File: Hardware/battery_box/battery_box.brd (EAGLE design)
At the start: 60 x 70 mm, 24 parts, among them IC1 LM2574N-5.0, U1 PIC16F506P

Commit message: Added Connectors to Schematic
Adds the DC Jacks and USB connectors and LEDs to the schematic for
mounting on PCB. Added comments to schematic and changed .gitignore
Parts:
- removed TB: 6WAYTB, inverter:TERMINAL_BLOCK
- removed X1: (no value), con-molex:22-23-2061
- added J1: CON_HEADER_PRG_PIC_ICSPA, equinox:HEADER_PRG_1X05
- added LD1: (no value), led:DUOLED-C-5MM
- added R6: (no value), rcl:R0805
- added X2: KUSBVX, con-kycon:KUSBVX
- U$2: value EQBX_PTCEQBX_PTC -> KYCON_KLDVX-0202; device eqbx_ptc:EQBX_PTC -> equinox:KYCON_KLVDX_2020_B
- U$3: value EQBX_FUSEEQBX_FUSE -> KYCON_KLDVX-0202; device eqbx_fuse:EQBX_FUSE -> equinox:KYCON_KLVDX_2020_B
- moved U$3 76.4 mm to (7.85, -22.1)
- moved U$2 64.5 mm to (7.85, -10.3), turned to 0 degrees
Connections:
- removed net N$10: U1.4, X1.1
- removed net N$14: R8.1, TB.P$6
- removed net N$19: TB.P$1, U$2.PTC-
- removed net N$5: U1.13, X1.4
- removed net N$6: CIN_PIC.1, D1.C, R13.1, U1.1, X1.2
- removed net N$7: U1.12, X1.5
- new net MCLR-: J1.1, U1.4
- new net PGC: J1.5, U1.12
- new net PGD: J1.4, U1.13
- new net VDD: CIN_PIC.1, D1.C, J1.2, R13.1, U1.1
- new net V_BATT: DCHARGE.NEGATIVE, PMOS.S, R1.2, R13.2, R4.1
- net GND: now also J1.3, LD1.C, R6.1, X2.4, X2.M1, X2.M2; no longer TB.P$4, X1.3
- net N$1: now also R6.2, U$2.2, U$2.3, U$3.2, U$3.3; no longer U$2.PTC+, U$3.-, U$3.-1
- net N$17: now also LD1.AR, R8.1; no longer COUT.1, IC1.1, INDUCTOR.P$2, TB.P$3
- net N$2: now also LD1.AX; no longer TB.P$5
- net N$20: now also U$2.1, U$3.1; no longer TB.P$2
- net N$4: now also COUT.1, IC1.1, INDUCTOR.P$2, X2.1; no longer DCHARGE.NEGATIVE, PMOS.S, R1.2, R13.2, R4.1, U$3.+, U$3.+1
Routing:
- net N$17: track 105.5 -> 0.00 mm
- net N$10: track 58.3 -> 0.00 mm
- net MCLR-: track 0.00 -> 57.5 mm
- net N$4: track 50.4 -> 0.00 mm
- net V_BATT: track 0.00 -> 48.5 mm
- net N$6: track 34.0 -> 0.00 mm
- net VDD: track 0.00 -> 32.7 mm
- net N$19: track 18.8 -> 0.00 mm
- net N$7: track 17.5 -> 0.00 mm
- net N$5: track 17.5 -> 0.00 mm
- net PGD: track 0.00 -> 16.3 mm
- net PGC: track 0.00 -> 16.3 mm
- net N$1: track 15.3 -> 0.00 mm
- net N$14: track 7.84 -> 0.00 mm
- net N$20: track 87.9 -> 86.8 mm

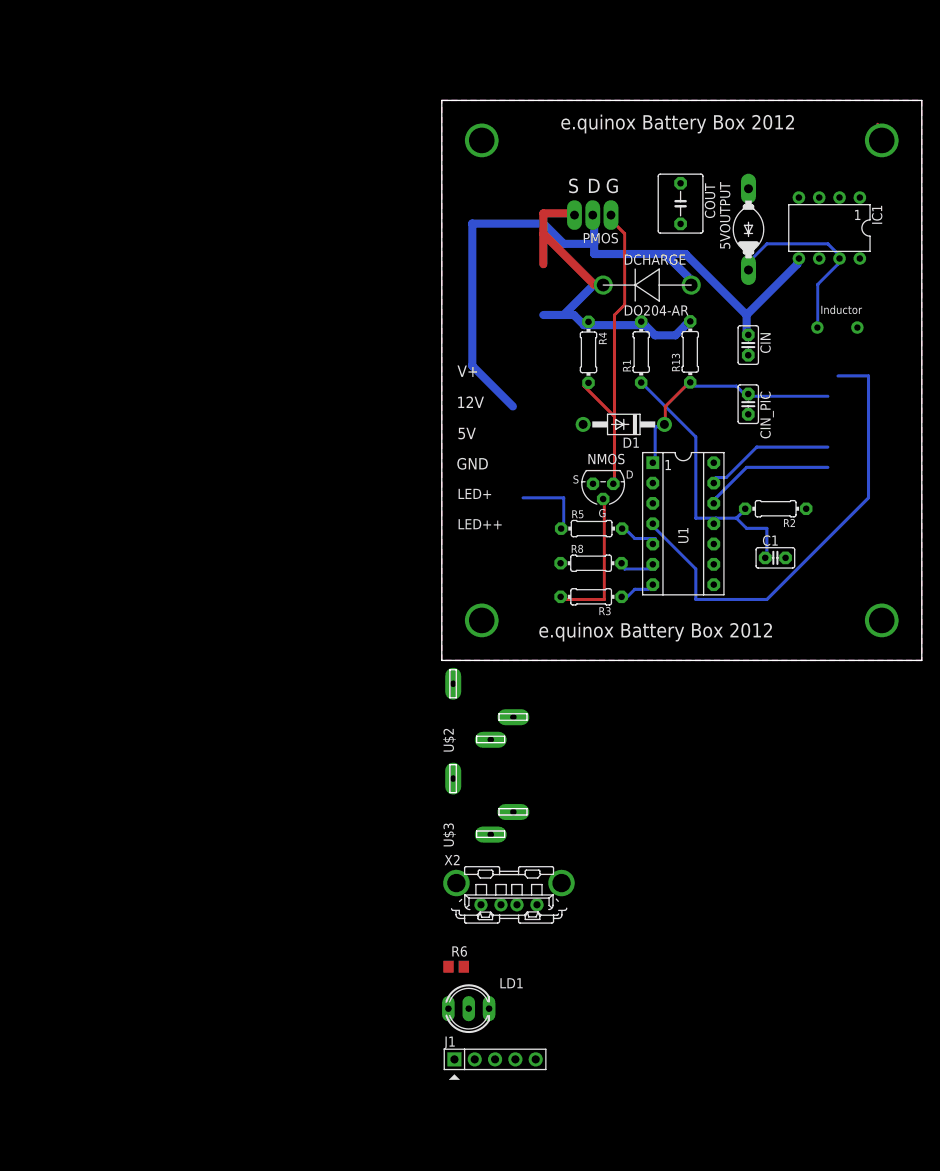
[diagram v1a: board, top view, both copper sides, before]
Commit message: Added cooments to fix problems identified
Problems identified during 2013 Jan trip have added as comments.
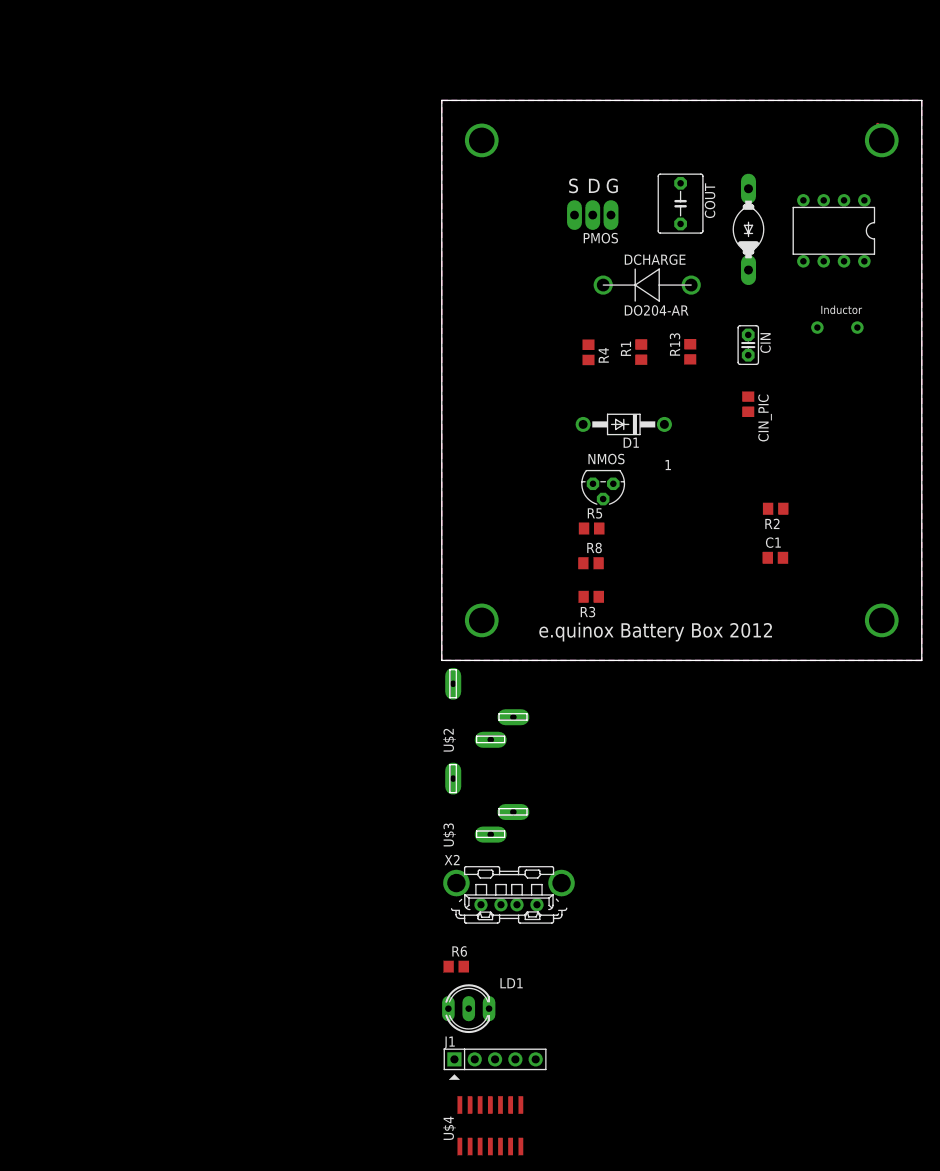
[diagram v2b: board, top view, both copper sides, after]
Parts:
- removed U1: PIC16F506P, microchip:DIP-14
- added U$4: PIC16F1503SOIC, equinox:SO-14
- C1: device capacitor-wima:C2.5-2 -> rcl:C0805
- CIN_PIC: value 22u -> 1u; device capacitor-wima:C2.5-2 -> rcl:C0805
- R1, R13, R2, R3, R4, R5, R8: device rcl:0204/7 -> rcl:R0805
- moved U$1 18.7 mm to (69.7, 12.5)
- moved IC1 0.66 mm to (49.0, 53.7)
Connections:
- removed net N$12: R3.1, U1.7
- new net N$5: R3.2, U$4.7
- net GND: now also U$4.14; no longer U1.14
- net MCLR-: no longer U1.4
- net N$13: now also R3.1; no longer R3.2
- net N$15: now also U$4.6; no longer U1.6
- net N$3: now also U$4.11; no longer U1.11
- net N$8: now also U$4.5; no longer U1.5
- net PGC: no longer U1.12
- net PGD: no longer U1.13
- net VDD: now also U$4.1; no longer U1.1
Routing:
- net N$20: track 86.8 -> 0.00 mm
- net MCLR-: track 57.5 -> 0.00 mm
- net V_BATT: track 48.5 -> 0.00 mm
- net N$9: track 40.8 -> 0.00 mm
- net N$3: track 36.0 -> 0.00 mm
- net VDD: track 32.7 -> 0.00 mm
- net N$11: track 24.1 -> 0.00 mm
- net N$13: track 18.5 -> 0.00 mm
- net PGD: track 16.3 -> 0.00 mm
- net PGC: track 16.3 -> 0.00 mm
- net N$2: track 9.21 -> 0.00 mm
- net N$12: track 5.49 -> 0.00 mm
- net N$8: track 5.41 -> 0.00 mm
- net N$15: track 5.28 -> 0.00 mm
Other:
- board text removed: "12V"
- board text removed: "5V"
- board text removed: "GND"
- board text removed: "LED+"
- board text removed: "LED++"
- board text removed: "V+"

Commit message: Added the Connector Test PCB
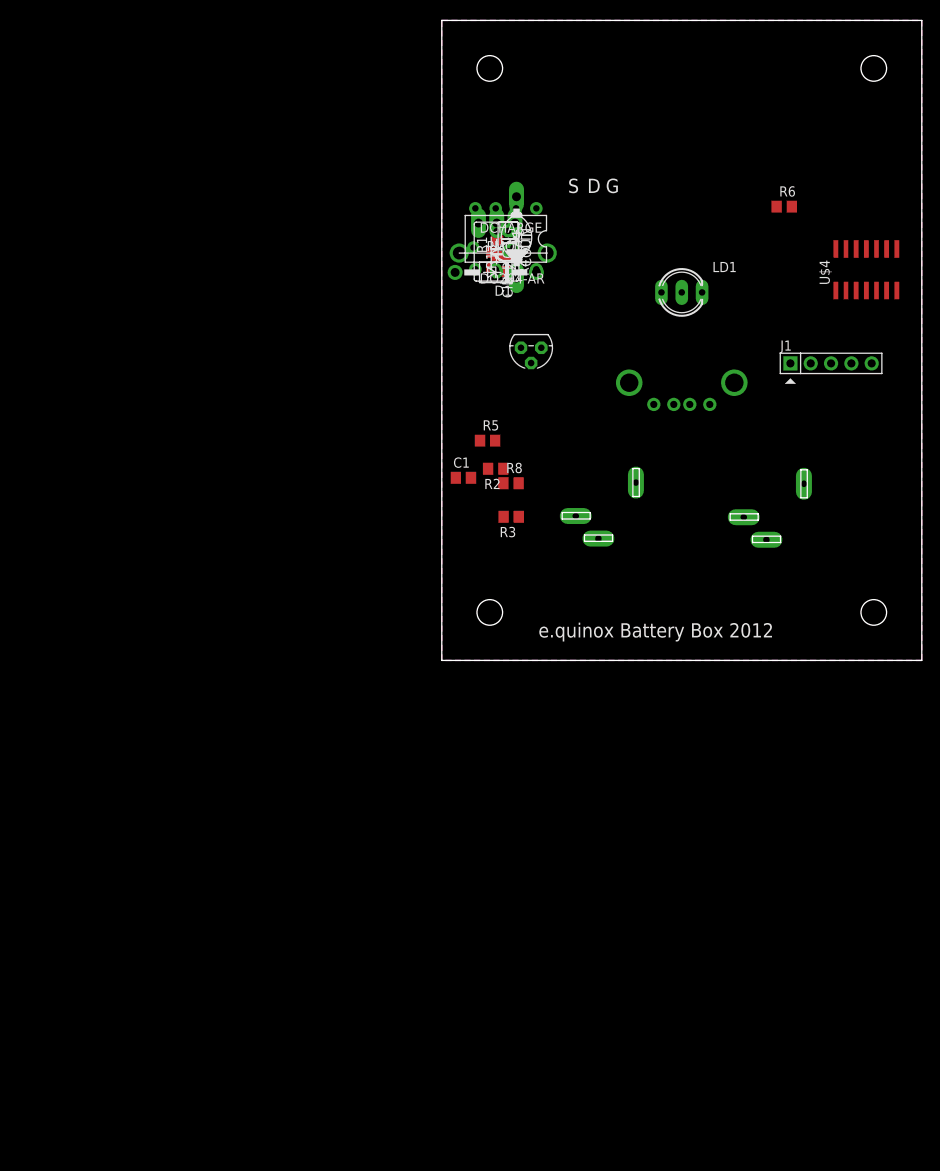
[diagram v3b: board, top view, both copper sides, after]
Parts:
- added U$5, U$6, U$7, U$8: PCB_MOUNT_RICHO, equinox:PCBMOUNT
- moved U$4 116.9 mm to (53.1, 48.8)
- moved R6 103.5 mm to (42.8, 56.7)
- moved J1 96.6 mm to (48.7, 37.1)
- moved LD1 93.4 mm to (30.0, 46.0)
- moved U$1 86.4 mm to (5.73, 70.5)
- moved X2 66.2 mm to (30.0, 32.0), flipped to the bottom
- moved INDUCTOR 44.1 mm to (6.45, 51.6)
- moved IC1 41.0 mm to (8.01, 52.7)
- moved C1 40.3 mm to (2.70, 22.8)
- moved U$2 39.8 mm to (38.9, 14.7), flipped to the bottom
- moved U$3 38.3 mm to (17.9, 14.9), flipped to the bottom
- moved CIN_PIC 36.7 mm to (6.31, 50.0)
- moved R2 35.4 mm to (6.74, 24.0)
- moved CIN 32.7 mm to (8.31, 52.4)
- moved 5VOUTPUT 29.0 mm to (9.34, 52.9)
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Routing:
- net N$18: track 1.50 -> 0.00 mm
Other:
- board size 60 x 70 mm -> 60 x 80 mm
- board text removed: "1"
- board text removed: "Inductor"

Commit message: Electronics added.
Should be first fully working prototype of 2013 unit. See README for
changes from 2012 version.
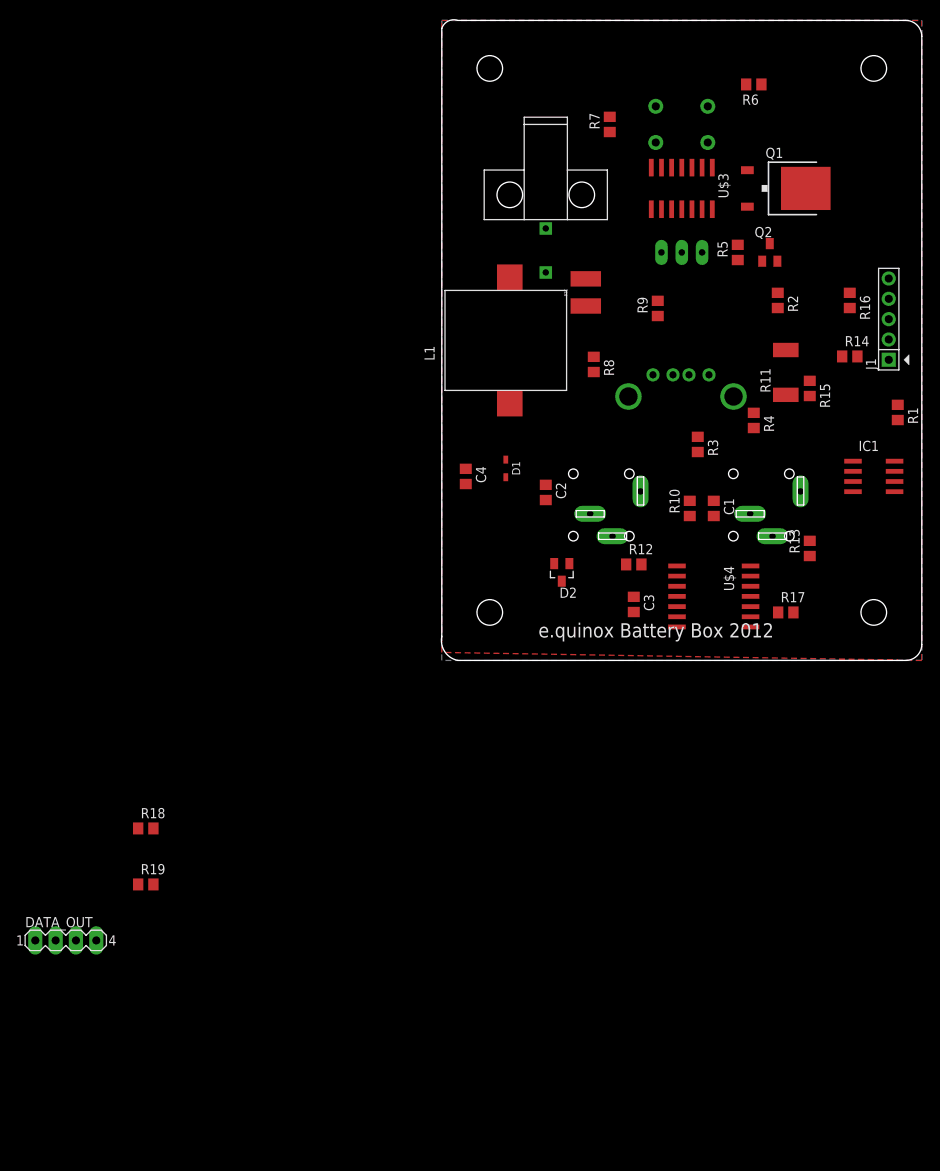
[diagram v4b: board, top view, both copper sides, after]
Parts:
- removed 5VOUTPUT: 1N5059, diode:DO204-10
- removed CIN: 22u, capacitor-wima:C2.5-2
- removed CIN_PIC: 1u, rcl:C0805
- removed COUT: 220uF, capacitor-wima:C5B5.5
- removed DCHARGE: DO204-AR, diode:DO204
- removed INDUCTOR: EQBX_INDUCTOR2, inductor:INDUCTOR
- removed NMOS: BSS101, transistor-fet:TO92
- removed PMOS: PMOS, PMOS:NMOS_IPAK
- added 12V_OUT_1, 12V_OUT_2: KYCON_KLDVX-0202, equinox:KYCON_KLVDX_2020_B
- added C2, C3, C4: 22u, rcl:C0805
- added D2: BAS40, diode:SOT23
- added DATA_OUT: (no value), con-lstb:MA04-1
- added L1: INDUCTOR, equinox:SMD_INDUCTOR
- added Q1: IRFR5505PBFTO252, equinox:TO252
- added Q2: BSS123, transistor-small-signal:SOT23
- added R10, R19: 10k, rcl:R0805
- added R11: 0.005, rcl:R2512
- added R12: 100k, rcl:R0805
- added R14, R15: 66k, rcl:R0805
- added R16, R17, R7: 1k, rcl:R0805
- added R18: 1M, rcl:R0805
- added R9: 20k, rcl:R0805
- added SW_POW: (no value), SparkFun:TACTILE-PTH
- added X1: CON_MOLEX_39_29_1028, equinox:MOLEX_39_29_1028
- C1: value 1u -> (none)
- D1: value 1N4004 -> 5.1V; device diode:DO41-10 -> zetex:SOD323
- IC1: value LM2574N-5.0 -> AD826R; device linear:DIL08 -> analog-devices:SO8
- R1: value 20k -> 75k
- R13: value 500 -> 100k
- R2: value 10k -> 49.9k
- R3: value 1k -> 75k
- R4: value 100k -> 49.9k
- R6: value (none) -> 1k
- R8: value 1k -> 500
- U$2: value KYCON_KLDVX-0202 -> PTC; device equinox:KYCON_KLVDX_2020_B -> equinox:MINISMDC260F
- U$3: value KYCON_KLDVX-0202 -> PIC16F1824; device equinox:KYCON_KLVDX_2020_B -> equinox:SO-14
- U$4: value PIC16F1503SOIC -> LM2574; device equinox:SO-14 -> equinox:SO14W
- moved U$1 109.6 mm to (-48.0, -25.0)
- moved IC1 54.7 mm to (54.0, 23.0), turned to 270 degrees
- moved R1 54.1 mm to (57.0, 31.0), turned to 270 degrees
- moved R13 52.0 mm to (46.0, 14.0)
- moved U$3 45.8 mm to (30.0, 59.0), flipped to the top, turned to 180 degrees
- moved U$4 45.1 mm to (34.0, 8.00), turned to 270 degrees
- moved R2 41.1 mm to (42.0, 45.0), turned to 270 degrees
- moved R5 39.1 mm to (37.0, 51.0), turned to 90 degrees
- moved U$2 37.6 mm to (18.0, 46.0), flipped to the top, turned to 90 degrees
- moved R4 36.3 mm to (39.0, 30.0)
- moved C1 31.5 mm to (34.0, 19.0), turned to 270 degrees
- moved R3 25.0 mm to (32.0, 27.0), turned to 270 degrees
- moved D1 24.5 mm to (8.00, 24.0), turned to 270 degrees
- moved R8 18.1 mm to (19.0, 37.0), turned to 270 degrees
- moved R6 15.7 mm to (39.0, 72.0), turned to 180 degrees
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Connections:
- removed net MCLR-: J1.1
- removed net N$13: NMOS.2, R3.1
- removed net N$4 (its old number): COUT.1, IC1.1, INDUCTOR.P$2, X2.1
- new net I_SENSE: IC1.1, R15.1, U$3.10
- new net MCLR_: J1.1, U$3.4
- new net N$10: R5.2, U$3.8
- new net N$12: Q2.1, R6.1
- new net N$14: R6.2, U$3.7
- new net N$16: IC1.2, R15.2, R17.2
- new net N$19: IC1.6, IC1.7, R14.2
- new net N$2: LD1.AR, R7.1
- new net N$6: U$2.P$1, X1.P$1
- new net N$7: R7.2, U$3.9
- new net POW: R19.1, SW_POW.1, SW_POW.2, U$3.2
- new net RX: DATA_OUT.3, U$3.5
- new net TX: DATA_OUT.2, U$3.6
- new net USB_OUT: C3.1, L1.P$2, R1.2, R3.2, U$4.3, X2.1
- net GND: now also C4.2, D1.2, DATA_OUT.1, Q2.2, R10.1, R11.1, R13.2, R17.1, SW_POW.3, SW_POW.4, U$3.14, X1.P$2; no longer 5VOUTPUT.A, CIN.2, CIN_PIC.2, COUT.2, D1.A, IC1.2, IC1.3, NMOS.1, R2.1, R6.1, U$4.14, X2.4, X2.M1, X2.M2
- net N$1: now also 12V_OUT_1.1, 12V_OUT_2.1, C2.1, Q1.3, U$4.10; no longer R6.2, U$2.2, U$2.3, U$3.2, U$3.3
- net N$11: now also Q1.1, Q2.3, R18.2; no longer 5VOUTPUT.C, IC1.7, INDUCTOR.P$1
- net N$15: now also IC1.3, R14.1, R16.2; no longer R8.2, U$4.6
- net N$17: now also IC1.5, R12.2, R13.1; no longer LD1.AR, R8.1
- net N$20: now also 12V_OUT_1.2, 12V_OUT_1.3, 12V_OUT_2.2, 12V_OUT_2.3, C2.2, C3.2, D2.1, R11.2, R16.1, R2.1, R4.1, U$4.4, U$4.5, U$4.6, X2.4, X2.M1, X2.M2; no longer CIN.1, DCHARGE.POSITIVE, IC1.5, PMOS.D, U$2.1, U$3.1
- net N$3: now also X2.3; no longer C1.1, U$4.11
- net N$5: now also R3.1, R4.2, X2.2; no longer R3.2, U$4.7
- net N$8: now also C1.1, R10.2, R9.1, U$3.11; no longer R5.2, U$4.5
- net N$9: now also D2.3, L1.P$1, U$4.12; no longer NMOS.3, PMOS.G, R4.2
- net PGC: now also U$3.12
- net PGD: now also U$3.13
- net VDD: now also C4.1, D1.1, DATA_OUT.4, IC1.8, R12.1, R19.2, R8.1, U$3.1; no longer CIN_PIC.1, D1.C, R13.1, U$4.1
- net V_BATT: now also Q1.2, R18.1, R8.2, R9.2, U$2.P$2; no longer DCHARGE.NEGATIVE, PMOS.S, R1.2, R13.2, R4.1
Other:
- board size 60 x 80 mm -> 60 x 80.1 mm
- board text added: "Check this!!!"
- board text removed: "D"
- board text removed: "G"
- board text removed: "S"

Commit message: Changed location op a mp power supply
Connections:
- net USB_OUT: now also IC1.8, R12.1
- net VDD: no longer IC1.8, R12.1
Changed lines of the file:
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@@
 <contactref element="C4" pad="1"/>
 <contactref element="R19" pad="2"/>
-<contactref element="IC1" pad="8"/>
-<contactref element="R12" pad="1"/>
 <contactref element="DATA_OUT" pad="4"/>
 <wire x1="19" y1="37.95" x2="33.81" y2="61.6" width="0" layer="19" extent="1-1"/>
 <wire x1="8" y1="25.1" x2="19" y2="37.95" width="0" layer="19" extent="1-1"/>
 <wire x1="3" y1="23.95" x2="8" y2="25.1" width="0" layer="19" extent="1-1"/>
-<wire x1="23.05" y1="12" x2="8" y2="25.1" width="0" layer="19" extent="1-1"/>
 <wire x1="55.87" y1="40.12" x2="33.81" y2="61.6" width="0" layer="19" extent="1-1"/>
-<wire x1="56.6" y1="24.905" x2="55.87" y2="40.12" width="0" layer="19" extent="1-1"/>
 <wire x1="-36.05" y1="-28" x2="3" y2="23.95" width="0" layer="19" extent="1-1"/>
 <wire x1="-43.19" y1="-35" x2="-36.05" y2="-28" width="0" layer="19" extent="1-1"/>
@@
 <contactref element="R3" pad="2"/>
 <contactref element="R1" pad="2"/>
+<contactref element="IC1" pad="8"/>
+<contactref element="R12" pad="1"/>
+<wire x1="56.6" y1="24.905" x2="57" y2="30.05" width="0" layer="19" extent="1-1"/>
 <wire x1="33.4" y1="35.7" x2="57" y2="30.05" width="0" layer="19" extent="1-1"/>
 <wire x1="32" y1="26.05" x2="33.4" y2="35.7" width="0" layer="19" extent="1-1"/>
-<wire x1="29.4" y1="9.27" x2="32" y2="26.05" width="0" layer="19" extent="1-1"/>
-<wire x1="24" y1="7.95" x2="29.4" y2="9.27" width="0" layer="19" extent="1-1"/>
+<wire x1="23.05" y1="12" x2="32" y2="26.05" width="0" layer="19" extent="1-1"/>
+<wire x1="24" y1="7.95" x2="23.05" y2="12" width="0" layer="19" extent="1-1"/>
+<wire x1="29.4" y1="9.27" x2="24" y2="7.95" width="0" layer="19" extent="1-1"/>
 <wire x1="8.5" y1="47.9" x2="33.4" y2="35.7" width="0" layer="19" extent="1-1"/>
 </signal>

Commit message: First PCB Layout
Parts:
- removed U$1: EQUINOX_LOGO_SMALL, equinox:EQUINOX_LOGO_SMALL
- moved DATA_OUT 135.9 mm to (30.0, 77.0)
- moved R19 125.6 mm to (39.0, 72.0), turned to 90 degrees
- moved R18 111.0 mm to (43.0, 56.0), turned to 90 degrees
- moved D1 48.4 mm to (23.0, 70.0), turned to 180 degrees
- moved C4 46.2 mm to (20.0, 66.0), turned to 180 degrees
- moved C1 24.3 mm to (38.0, 43.0)
- moved R10 24.2 mm to (34.0, 43.0)
- moved R17 24.2 mm to (46.0, 30.0), turned to 270 degrees
- moved R5 18.0 mm to (19.0, 52.0)
- moved R13 16.5 mm to (42.0, 30.0)
- moved R7 15.1 mm to (23.0, 52.0)
- moved R8 10.3 mm to (24.0, 46.0)
- moved R4 10.0 mm to (33.0, 22.0)
- moved Q2 9.00 mm to (41.0, 60.0), turned to 270 degrees
- moved R6 8.06 mm to (43.0, 65.0)
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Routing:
- net N$20: track 0.00 -> 137.6 mm
- net VDD: track 0.00 -> 119.8 mm, vias 0 -> 3
- net N$1: track 0.00 -> 105.9 mm, vias 0 -> 2
- net N$19: track 0.00 -> 104.7 mm, vias 0 -> 2
- net USB_OUT: track 0.00 -> 99.5 mm, vias 0 -> 2
- net GND: track 0.00 -> 79.9 mm, vias 0 -> 3
- net N$3: track 0.00 -> 74.6 mm, vias 0 -> 4
- net MCLR_: track 0.00 -> 59.4 mm, vias 0 -> 2
- net N$9: track 0.00 -> 58.1 mm
- net I_SENSE: track 0.00 -> 55.0 mm, vias 0 -> 2
- net N$17: track 0.00 -> 53.5 mm, vias 0 -> 3
- net N$8: track 0.00 -> 47.1 mm, vias 0 -> 2
- net V_BATT: track 0.00 -> 37.0 mm, vias 0 -> 2
- net N$15: track 0.00 -> 35.8 mm
- net POW: track 0.00 -> 32.3 mm
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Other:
- board text removed: "Check this!!!"
